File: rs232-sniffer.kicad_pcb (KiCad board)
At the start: 2 copper layers, 125 x 150 mm, 161 parts, among them J101 DB9_Female, J102 Stiftleiste 2x9, J103 DB9_Male, J104 Stiftleiste 2x9, J2001 Stiftleiste 2x9, J2002 Buchsenleiste 1x6, horizontal, J2003 Stiftleiste 2x9, J2101 USB-C/16p, J2401 Stiftleiste 2x9, J2402 Buchsenleiste 1x6, horizontal, J2403 Stiftleiste 2x9, J2501 USB-C/16p, SW101 DIP-Switch 8, SW2001 DIP-Switch 8, SW2401 DIP-Switch 8, U101 AMS1117-3.3, U2101 CH340C, U2201 MAX3232, U2301 MAX3232, U2501 CH340C, U2601 MAX3232, U2701 MAX3232

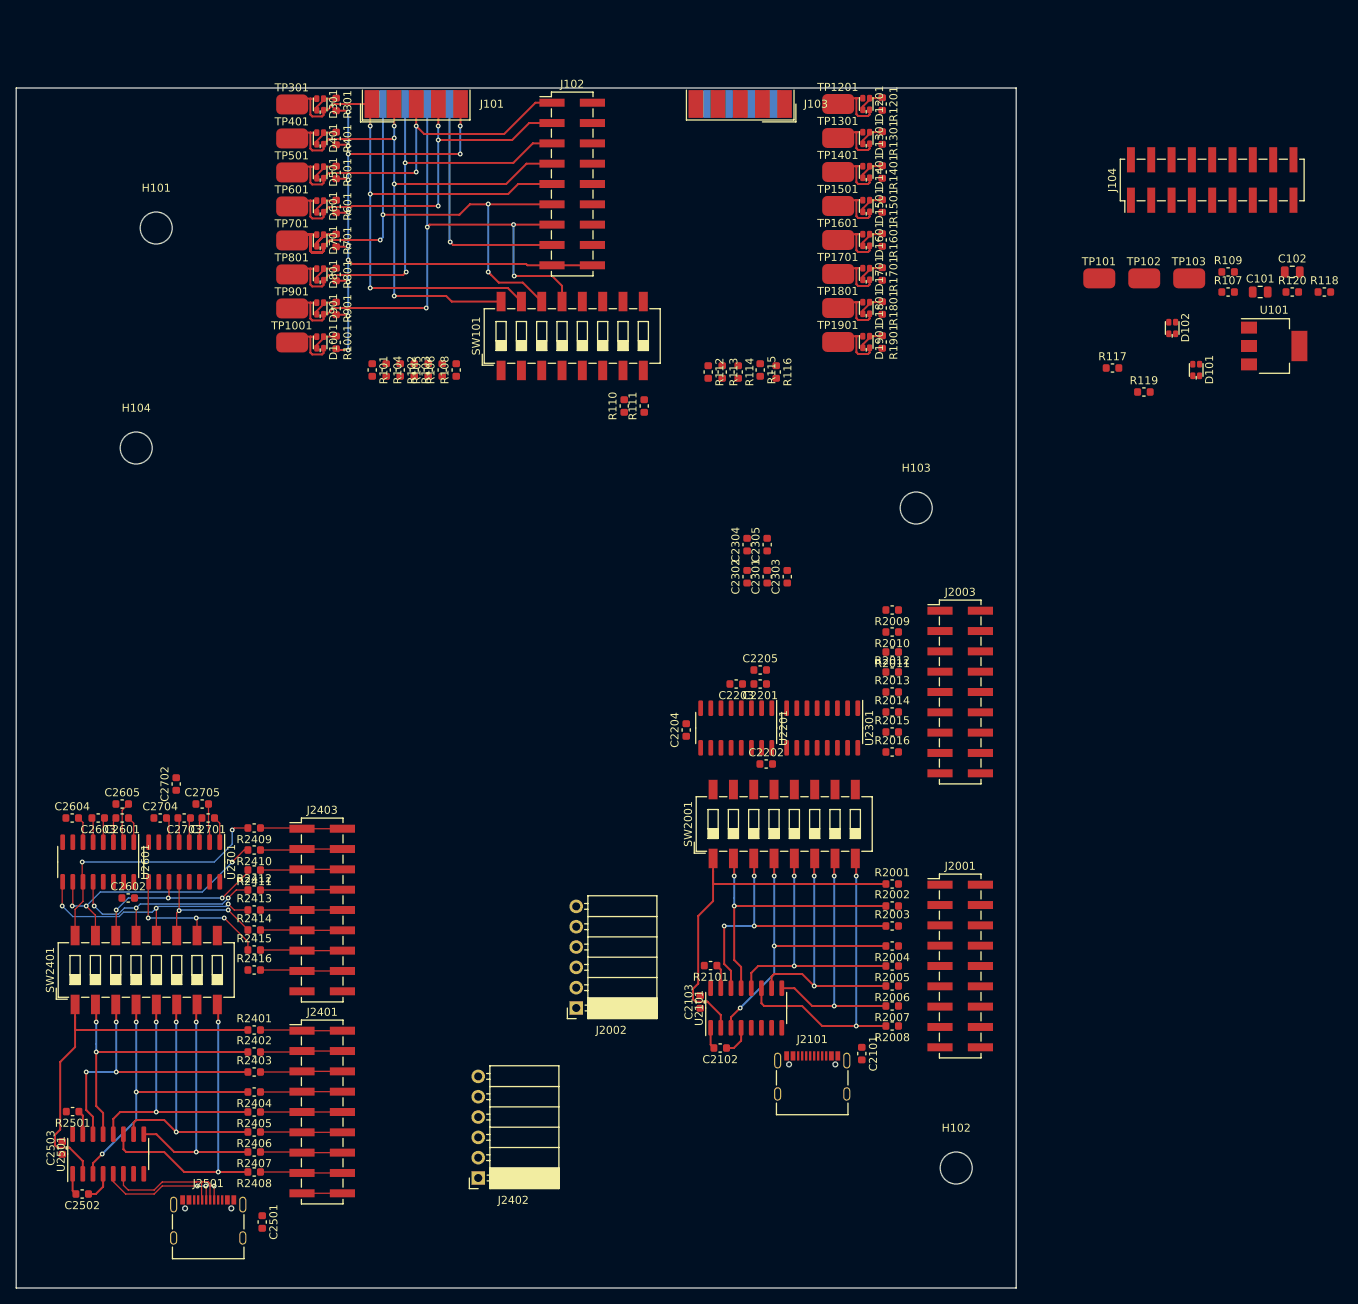
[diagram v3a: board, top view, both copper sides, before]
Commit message: Layout fast fertig Footprint für 2x9-polig wurde aktualisiert
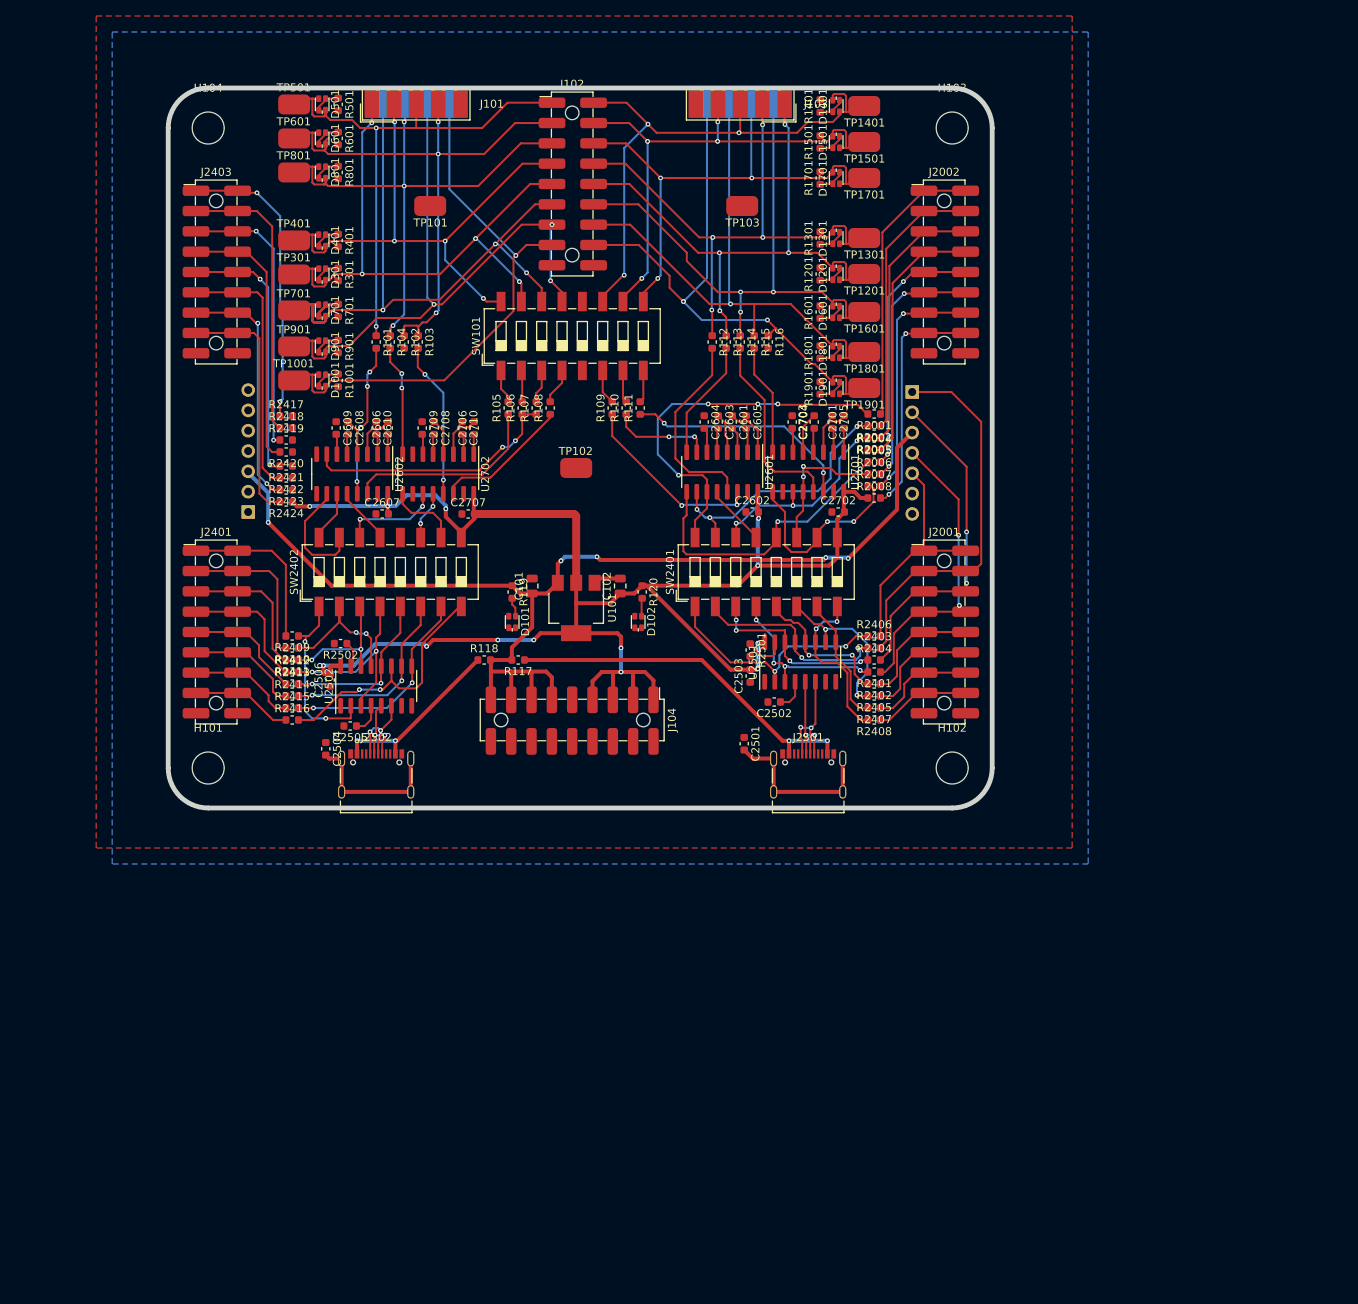
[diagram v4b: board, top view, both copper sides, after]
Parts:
- removed the J2002 at (85.0, 155.0)
- removed the J2501 at (39.0, 181.5)
- added J2402: Buchsenleiste 1x6, horizontal, Connector_PinSocket_2.54mm:PinSocket_1x07_P2.54mm_Horizontal, B.Cu at (127.0, 78.0)
- added J2502: USB-C/16p, htl_connectors:USB_C_Receptacle_LCSC_C167321, F.Cu at (60.0, 125.8)
- J102, J104, J2001, J2401, J2403: footprint Connector_PinHeader_2.54mm:PinHeader_2x09_P2.54mm_Vertical_SMD -> htl_connectors:PinHeader_2x09_P2.54mm_Vertical_SMD_LCSC_C88175
- J2002: renamed from J2003; footprint Connector_PinHeader_2.54mm:PinHeader_2x09_P2.54mm_Vertical_SMD -> htl_connectors:PinHeader_2x09_P2.54mm_Vertical_SMD_LCSC_C88175
- J2405: renamed from J2402; footprint Connector_PinSocket_2.54mm:PinSocket_1x06_P2.54mm_Horizontal -> Connector_PinSocket_2.54mm:PinSocket_1x07_P2.54mm_Horizontal; moved to B.Cu
- moved R118 114.7 mm to (73.5, 111.5)
- moved J104 104.7 mm to (84.5, 119.0), turned to 270 degrees
- moved C101 98.1 mm to (79.5, 102.2), turned to 90 degrees
- moved U101 93.2 mm to (85.0, 105.0), turned to 270 degrees
- moved C102 92.7 mm to (90.5, 102.2), turned to 90 degrees
- moved D101 91.1 mm to (77.0, 106.8)
- moved R120 89.5 mm to (93.2, 103.0), turned to 270 degrees
- moved J2405 88.1 mm to (44.0, 93.0), turned to 0 degrees
- moved R107 87.7 mm to (80.0, 80.0), turned to 90 degrees
- moved TP101 84.1 mm to (66.8, 54.8), turned to 180 degrees
- moved R119 82.8 mm to (77.0, 103.0), turned to 270 degrees
- moved R117 82.8 mm to (77.8, 111.5), turned to 180 degrees
- moved J2403 80.8 mm to (40.0, 63.0)
- moved R109 78.8 mm to (89.5, 80.0), turned to 90 degrees
- moved D102 76.2 mm to (92.8, 106.8)
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- renumbered C2101 to C2501, C2102 to C2502, C2103 to C2503, C2501 to C2504, C2502 to C2505, C2503 to C2506, C2201 to C2601, C2202 to C2602, C2203 to C2603, C2204 to C2604, C2205 to C2605, C2601 to C2606, C2602 to C2607, C2603 to C2608, C2604 to C2609, C2605 to C2610, C2301 to C2701, C2302 to C2702, C2303 to C2703, C2304 to C2704, C2305 to C2705, C2701 to C2706, C2702 to C2707, C2703 to C2708, C2704 to C2709, C2705 to C2710, J2101 to J2501, R2009 to R2001, R2010 to R2002, R2011 to R2003, R2012 to R2004, R2013 to R2005, R2014 to R2006, R2015 to R2007, R2016 to R2008, R2004 to R2401, R2005 to R2402, R2002 to R2403, R2003 to R2404, R2006 to R2405, R2001 to R2406, R2007 to R2407, R2008 to R2408, R2401 to R2409, R2402 to R2410, R2403 to R2411, R2404 to R2412, R2405 to R2413, R2406 to R2414, R2407 to R2415, R2408 to R2416, R2409 to R2417, R2410 to R2418, R2411 to R2419, R2412 to R2420, R2413 to R2421, R2414 to R2422, R2415 to R2423, R2416 to R2424, R2101 to R2501, R2501 to R2502, SW2001 to SW2401, SW2401 to SW2402, U2101 to U2501, U2501 to U2502, U2201 to U2601, U2601 to U2602, U2301 to U2701, U2701 to U2702
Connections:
- D1001 pad 2: GND -> /LEDs A/Signal9
- D1001 pad 3: GND -> /LEDs A/Signal9
- J101 pad 9: Net-(J101-Pad9) -> /LEDs A/Signal9
- J102 pad 15: Net-(J101-Pad9) -> /LEDs A/Signal9
- J104 pad 1: +5V -> +3V3
- J104 pad 11: +3V3 -> +5V
- J104 pad 13: +3V3 -> +5V
- J104 pad 15: +3V3 -> +5V
- J104 pad 17: +3V3 -> +5V
- J104 pad 3: +5V -> +3V3
- J104 pad 5: +5V -> +3V3
- J104 pad 7: +5V -> +3V3
- TP1001 pad 1: GND -> /LEDs A/Signal9
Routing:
- net +3V3: track 0.00 -> 208.6 mm, vias 0 -> 13
- net +5V: track 0.00 -> 141.1 mm, vias 0 -> 5
- net GND: track 111.6 -> 3.92 mm, vias 12 -> 0
- net /LEDs A/Signal9: track 0.00 -> 69.7 mm, vias 0 -> 1
- net /LEDs B/Signal8: track 7.79 -> 73.0 mm, vias 0 -> 1
- net /LEDs B/Signal9: track 7.79 -> 72.9 mm, vias 0 -> 2
- net /LEDs B/Signal6: track 7.79 -> 72.8 mm, vias 0 -> 3
- net /LEDs B/Signal1: track 7.79 -> 71.6 mm, vias 0 -> 4
- net /LEDs B/Signal2: track 7.79 -> 70.8 mm, vias 0 -> 4
- net /LEDs B/Signal3: track 7.79 -> 69.7 mm, vias 0 -> 3
- net /LEDs B/Signal7: track 7.79 -> 65.4 mm, vias 0 -> 3
- net /LEDs B/Signal4: track 7.79 -> 64.9 mm, vias 0 -> 4
- net Net-(J2001-Pad3): track 0.00 -> 47.9 mm
- net /UART Hub R/UART - RS232 1/UART_Tx1: track 0.00 -> 47.3 mm, vias 0 -> 4
- net /UART Hub R/USB-Power: track 0.00 -> 45.3 mm, vias 0 -> 2
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- added copper zone on B.Cu, net GND
- added copper zone on F.Cu, net GND
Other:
- board size 125 x 150 mm -> 103 x 90 mm
- board text added: "V20.0.0"
